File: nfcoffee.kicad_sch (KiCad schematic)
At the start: 17 parts, among them J1 Conn_Buzz, J3 Conn_SD_Shield_Left, J4 Conn_SD_Shiled_Right, J5 Conn_OLED, J6 Conn_PN532_NFC, Q1 BSS123, U1 WEMOS_D1_mini

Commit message: added SD card to PCB on the wrong layer
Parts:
- removed J3: Conn_SD_Shield_Left, Connector_PinSocket_2.54mm:PinSocket_1x08_P2.54mm_Vertical, symbol Connector:Conn_01x08_Socket
- removed J4: Conn_SD_Shiled_Right, Connector_PinSocket_2.54mm:PinSocket_1x08_P2.54mm_Vertical, symbol Connector:Conn_01x08_Socket
- added C1: 100nF, Capacitor_SMD:C_1206_3216Metric_Pad1.33x1.80mm_HandSolder, symbol Device:C
- added MICRO_SD1: MICRO_SD(TFC-9P-1.xH(ATFFS150A01BR016)), olimex:J_SD_Card-micro_socket_A, symbol microsd:MICRO_SD(TFC-9P-1.xH(ATFFS150A01BR016))
- J5: footprint Connector_PinHeader_2.54mm:PinHeader_1x04_P2.54mm_Vertical -> Connector_PinSocket_2.54mm:PinSocket_1x04_P2.54mm_Vertical
- J6: footprint Connector_PinHeader_2.54mm:PinHeader_1x08_P2.54mm_Vertical -> Connector_PinSocket_2.54mm:PinSocket_1x08_P2.54mm_Vertical
- RD1: value R -> 10k
- RD2: value R -> 4k7
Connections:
- net 3V3: now also C1.1, MICRO_SD1.4 (VDD)
- net GND: now also C1.2, MICRO_SD1.6 (GND), MICRO_SD1.SH (Card_Housing)
- net GPIO12: now also MICRO_SD1.7 (DAT0/DO)
- net GPIO13: now also MICRO_SD1.3 (CMD/DI)
- net GPIO14: now also MICRO_SD1.5 (CLK/SCLK)
- net GPIO2: now also MICRO_SD1.2 (CD/DAT3/CS)
- no-connect marks 0 -> 3

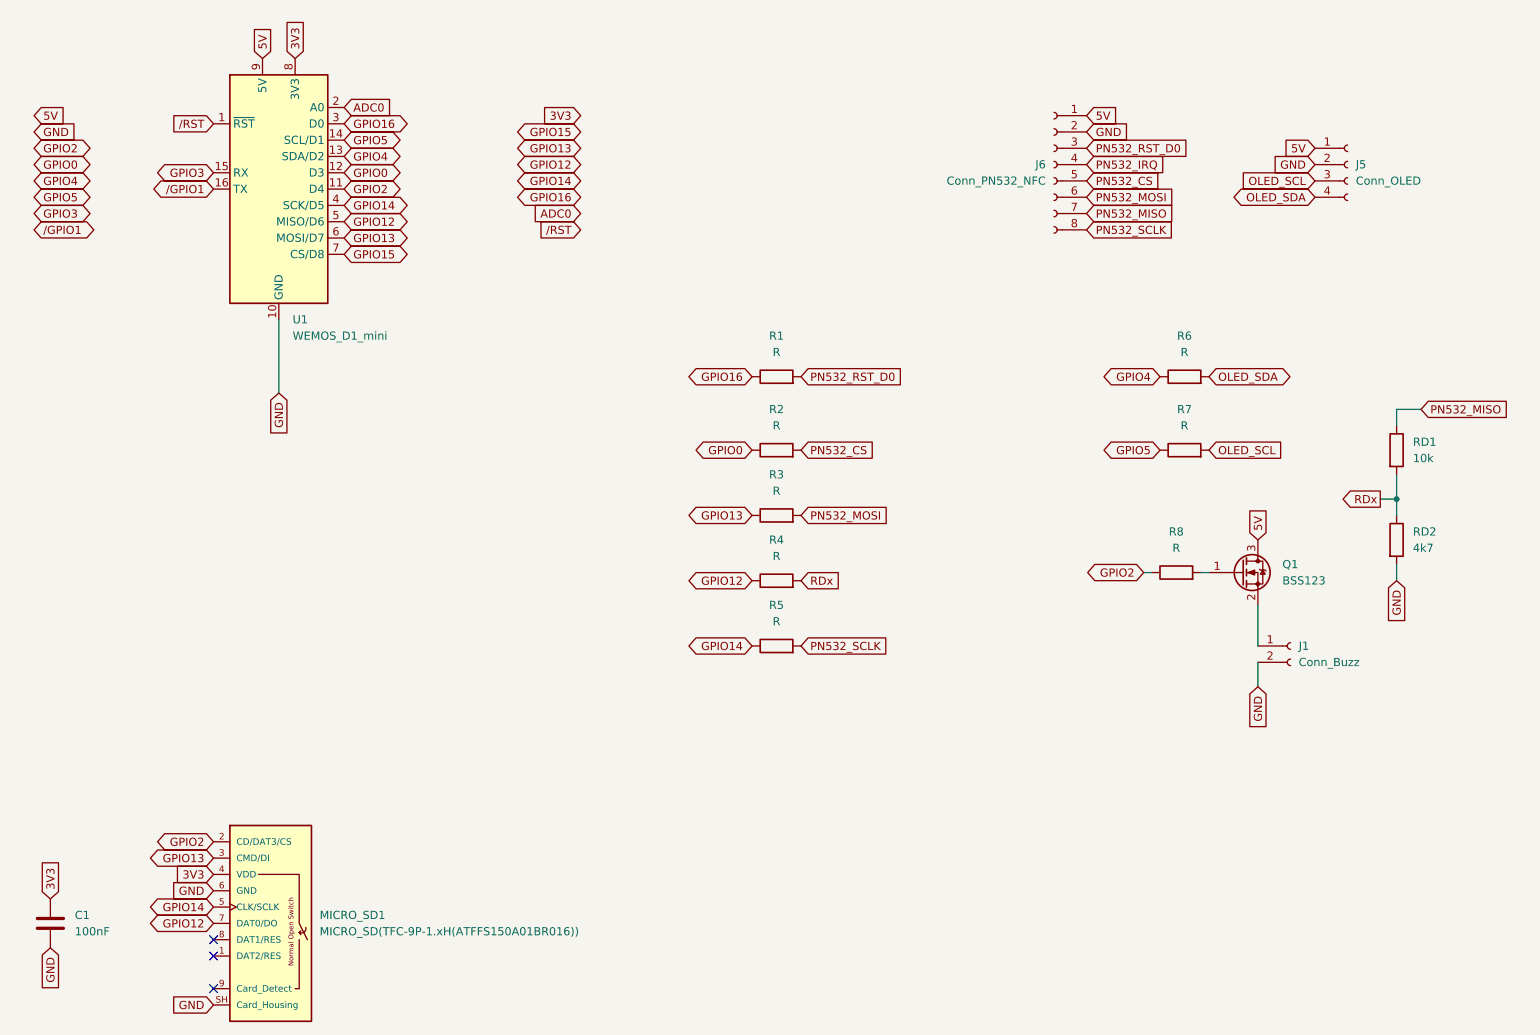
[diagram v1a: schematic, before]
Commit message: Removed SD Shield and replaced with a SD Card Connector directly. Removed current limiting resistors.
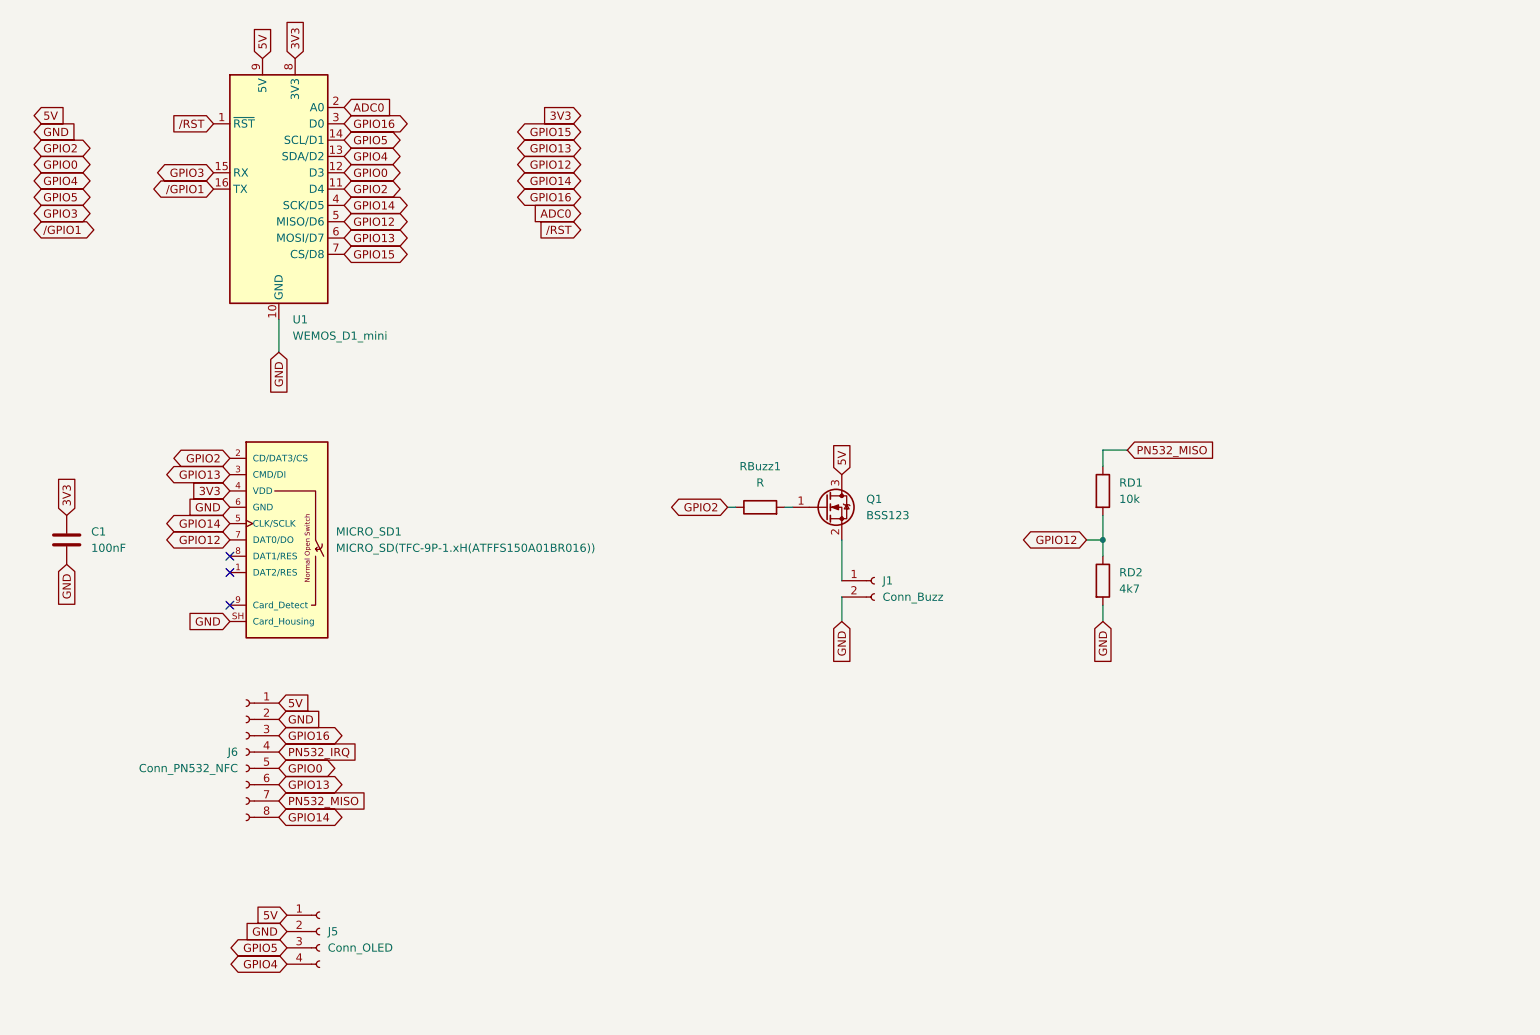
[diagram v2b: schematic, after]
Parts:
- removed R1, R2, R3, R4, R5, R6, R7: R, Resistor_SMD:R_1206_3216Metric_Pad1.30x1.75mm_HandSolder, symbol Device:R
- renumbered R8 to RBuzz1
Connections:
- net OLED_SCL is gone; now on net GPIO5: J5.3 (Pin_3)
- net OLED_SDA is gone; now on net GPIO4: J5.4 (Pin_4)
- net PN532_CS is gone; now on net GPIO0: J6.5 (Pin_5)
- net PN532_MOSI is gone; now on net GPIO13: J6.6 (Pin_6)
- net PN532_RST_D0 is gone; now on net GPIO16: J6.3 (Pin_3)
- net PN532_SCLK is gone; now on net GPIO14: J6.8 (Pin_8)
- net RDx is gone; now on net GPIO12: RD1.2, RD2.1
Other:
- moved on the sheet: C1, J1, J5, J6, MICRO_SD1, Q1, RBuzz1, RD1, RD2

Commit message: Version 5.1 - fixed the connection for the SD card chipselect, moved to GPIO15; - added 22 ohm resistor at the start of SPI CLK line; -removed the voltage divisor for PN532 CIPO because the SPI works on 3V3 anyway; - connected the SPI lines in a chain (not star) topo. From ESP8266 to the SD card and then to the PN532; - added production files for JLCPCB generated by the JLCPCB plug-in; - added DRU file for JLCPCB.
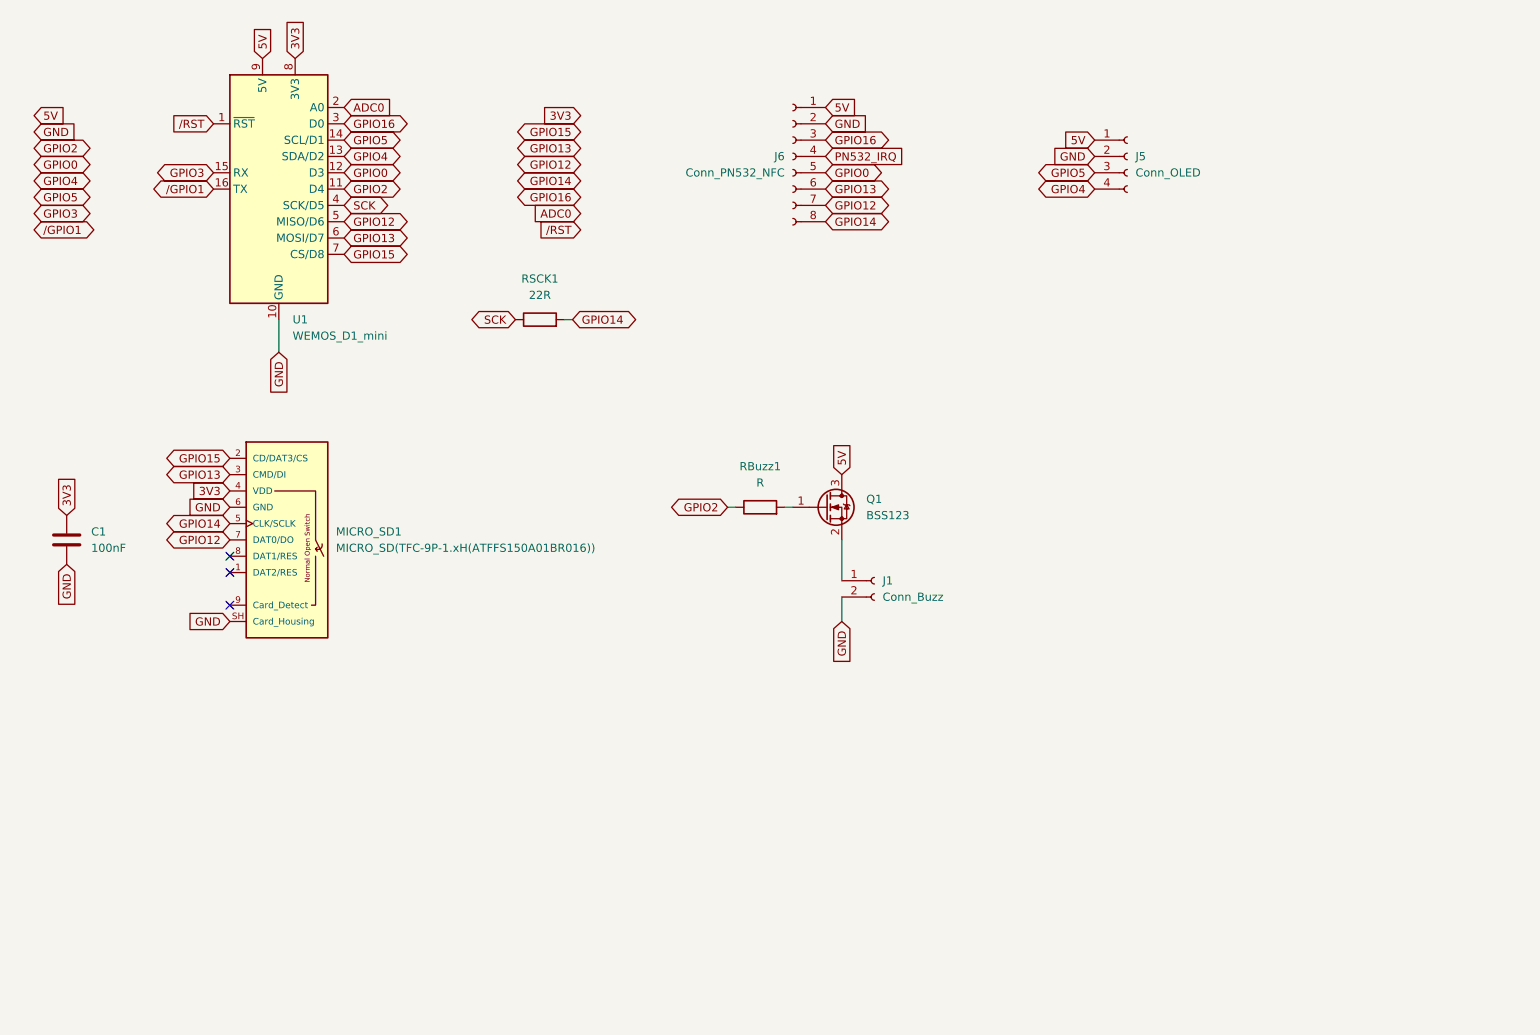
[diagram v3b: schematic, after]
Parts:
- removed RD1: 10k, Resistor_SMD:R_1206_3216Metric_Pad1.30x1.75mm_HandSolder, symbol Device:R
- removed RD2: 4k7, Resistor_SMD:R_1206_3216Metric_Pad1.30x1.75mm_HandSolder, symbol Device:R
- added RSCK1: 22R, Resistor_SMD:R_1206_3216Metric_Pad1.30x1.75mm_HandSolder, symbol Device:R
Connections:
- net PN532_MISO is gone; now on net GPIO12: J6.7 (Pin_7)
- net GPIO14: now also RSCK1.2; no longer U1.4 (SCK/D5)
- net GPIO15: now also MICRO_SD1.2 (CD/DAT3/CS)
- net GPIO2: no longer MICRO_SD1.2 (CD/DAT3/CS)
- new net SCK: RSCK1.1, U1.4 (SCK/D5)
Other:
- moved on the sheet: J5, J6
